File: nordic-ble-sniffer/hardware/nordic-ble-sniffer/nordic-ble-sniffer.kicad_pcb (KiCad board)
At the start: 2 copper layers, 8 parts, among them U1 NRF52840-QFAA-F-R7, U2 nRF52840, Y1 Crystal

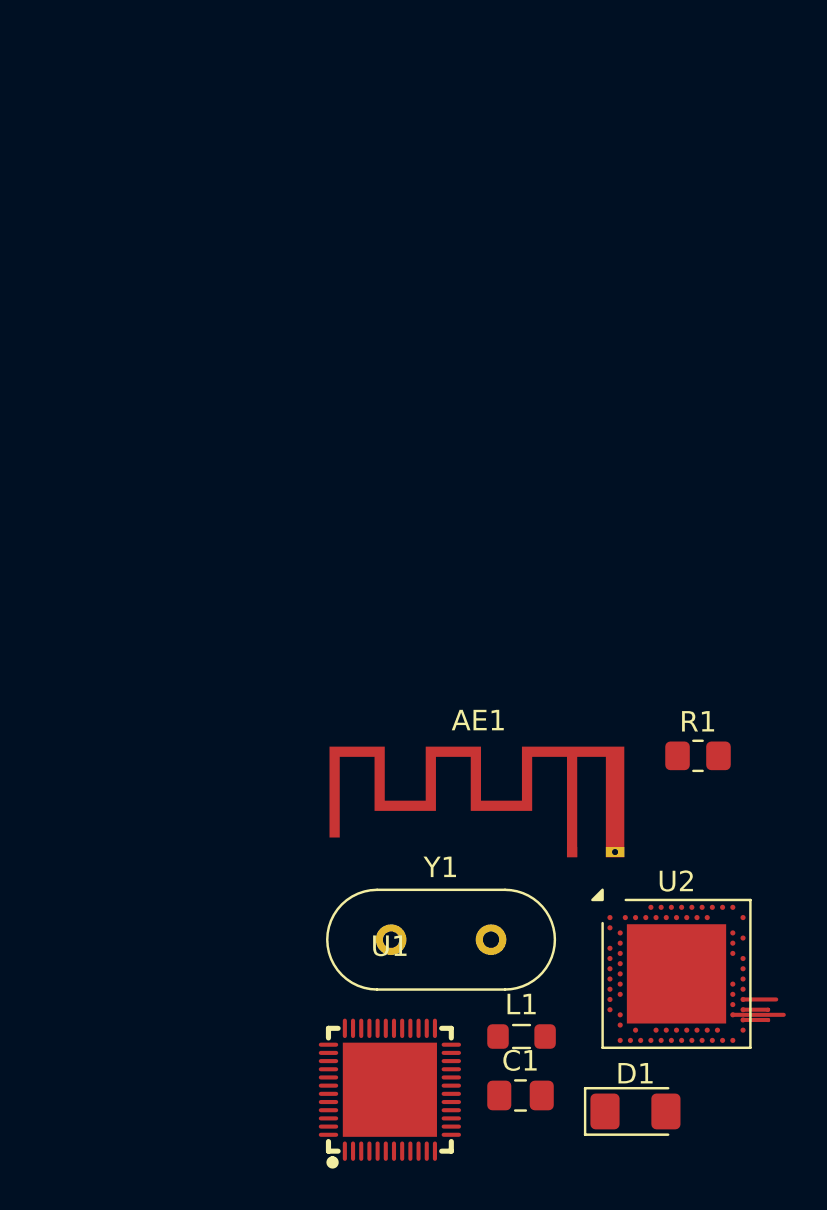
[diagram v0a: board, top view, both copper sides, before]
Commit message: finish schematic ble sniffer with nrf52833 qfn40
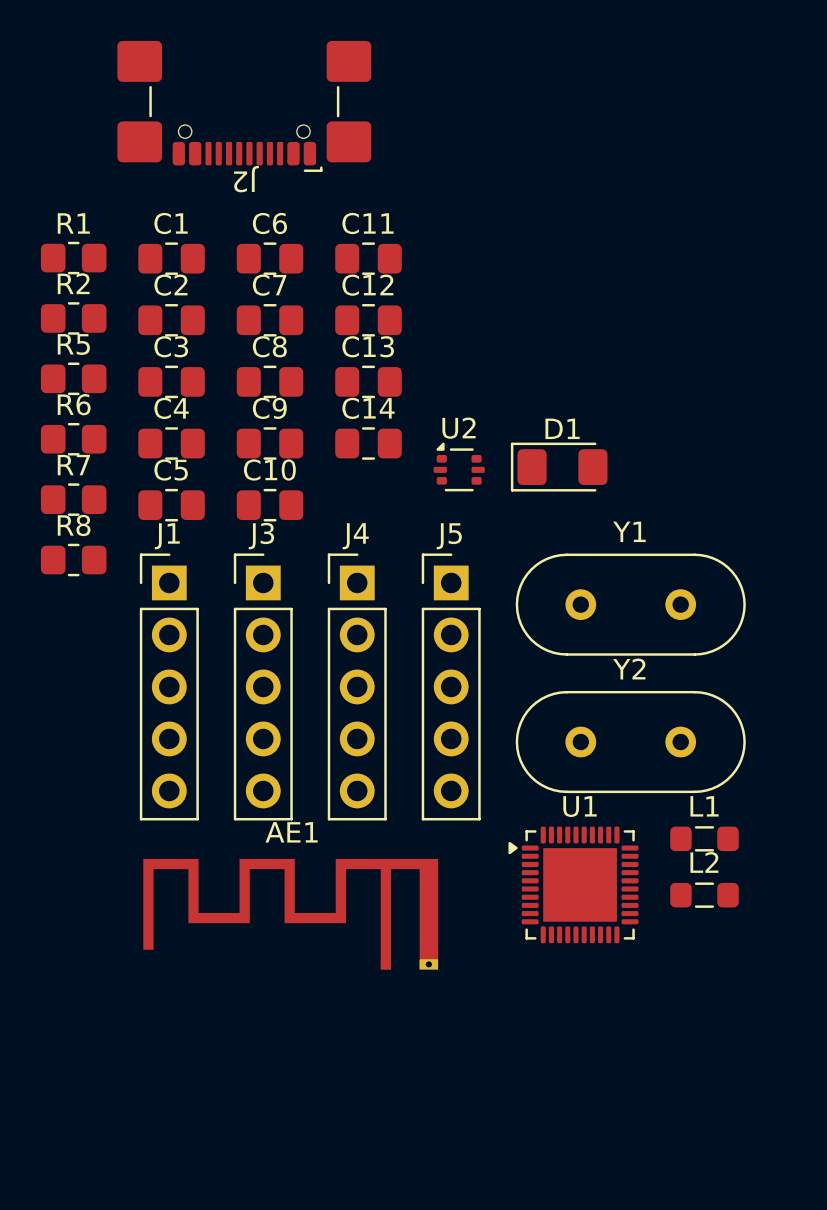
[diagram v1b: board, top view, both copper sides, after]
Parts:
- added C10: 4.7uF, Capacitor_SMD:C_0805_2012Metric_Pad1.18x1.45mm_HandSolder, F.Cu at (104.3, 63.7)
- added C11: 12pF, Capacitor_SMD:C_0805_2012Metric_Pad1.18x1.45mm_HandSolder, F.Cu at (109.1, 51.7)
- added C12: 12pF, Capacitor_SMD:C_0805_2012Metric_Pad1.18x1.45mm_HandSolder, F.Cu at (109.1, 54.7)
- added C13: 100nF, Capacitor_SMD:C_0805_2012Metric_Pad1.18x1.45mm_HandSolder, F.Cu at (109.1, 57.7)
- added C14: 100nF, Capacitor_SMD:C_0805_2012Metric_Pad1.18x1.45mm_HandSolder, F.Cu at (109.1, 60.7)
- added C2: 12pF, Capacitor_SMD:C_0805_2012Metric_Pad1.18x1.45mm_HandSolder, F.Cu at (99.5, 54.7)
- added C3: 12pF, Capacitor_SMD:C_0805_2012Metric_Pad1.18x1.45mm_HandSolder, F.Cu at (99.5, 57.7)
- added C4: 1pF, Capacitor_SMD:C_0805_2012Metric_Pad1.18x1.45mm_HandSolder, F.Cu at (99.5, 60.7)
- added C5: 1.2pF, Capacitor_SMD:C_0805_2012Metric_Pad1.18x1.45mm_HandSolder, F.Cu at (99.5, 63.7)
- added C6: 100nF, Capacitor_SMD:C_0805_2012Metric_Pad1.18x1.45mm_HandSolder, F.Cu at (104.3, 51.7)
- added C7: 820pF, Capacitor_SMD:C_0805_2012Metric_Pad1.18x1.45mm_HandSolder, F.Cu at (104.3, 54.7)
- added C8: 4.7uF, Capacitor_SMD:C_0805_2012Metric_Pad1.18x1.45mm_HandSolder, F.Cu at (104.3, 57.7)
- added C9: 4.7uF, Capacitor_SMD:C_0805_2012Metric_Pad1.18x1.45mm_HandSolder, F.Cu at (104.3, 60.7)
- added J1: gconn, Connector_PinHeader_2.54mm:PinHeader_1x05_P2.54mm_Vertical, F.Cu at (99.3, 67.5)
- added J2: USB2UART, Connector_USB:USB_C_Receptacle_GCT_USB4110, F.Cu at (103.0, 42.9)
- added J3: swd, Connector_PinHeader_2.54mm:PinHeader_1x05_P2.54mm_Vertical, F.Cu at (103.9, 67.5)
- added J4: gconn, Connector_PinHeader_2.54mm:PinHeader_1x05_P2.54mm_Vertical, F.Cu at (108.5, 67.5)
- added J5: gconn, Connector_PinHeader_2.54mm:PinHeader_1x05_P2.54mm_Vertical, F.Cu at (113.1, 67.5)
- added L2: 2.2nH, Inductor_SMD:L_0805_2012Metric_Pad1.05x1.20mm_HandSolder, F.Cu at (125.5, 82.8)
- added R2: 4K7, Resistor_SMD:R_0805_2012Metric_Pad1.20x1.40mm_HandSolder, F.Cu at (94.7, 54.6)
- added R5: 5K1, Resistor_SMD:R_0805_2012Metric_Pad1.20x1.40mm_HandSolder, F.Cu at (94.7, 57.6)
- added R6: 5K1, Resistor_SMD:R_0805_2012Metric_Pad1.20x1.40mm_HandSolder, F.Cu at (94.7, 60.5)
- added R7: 22 / 33, Resistor_SMD:R_0805_2012Metric_Pad1.20x1.40mm_HandSolder, F.Cu at (94.7, 63.5)
- added R8: 22 / 33, Resistor_SMD:R_0805_2012Metric_Pad1.20x1.40mm_HandSolder, F.Cu at (94.7, 66.4)
- added Y2: 32.768kHz, Crystal:Crystal_HC49-U_Vertical, F.Cu at (119.4, 75.3)
- C1: value C -> 100nF
- D1: value LED -> RED
- L1: value L -> 4.7nH
- R1: value R_US -> 10K
- U1: value NRF52840-QFAA-F-R7 -> nRF52833_QDxx; footprint easyeda2kicad:WQFN-48_L6.0-W6.0-P0.40-BL-EP4.6 -> Package_DFN_QFN:QFN-40-1EP_5x5mm_P0.4mm_EP3.6x3.6mm
- U2: value nRF52840 -> USBLC6-2P6; footprint Package_DFN_QFN:Nordic_AQFN-73-1EP_7x7mm_P0.5mm -> Package_TO_SOT_SMD:SOT-666
- Y1: value Crystal -> 32MHz
- moved C1 44.3 mm to (99.5, 51.7)
- moved R1 39.0 mm to (94.7, 51.7)
- moved D1 31.7 mm to (118.5, 61.9)
- moved U2 26.8 mm to (113.5, 62.0)
- moved Y1 18.8 mm to (119.4, 68.6)
- moved U1 13.7 mm to (119.4, 82.3)
- moved L1 13.2 mm to (125.5, 80.0)
- moved AE1 10.6 mm to (109.9, 86.2)
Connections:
- AE1 pad 1: unconnected-(AE1-A-Pad1) -> Net-(AE1-A)
- C1 pad 1: unconnected-(C1-Pad1) -> Net-(U1-DEC1)
- C1 pad 2: unconnected-(C1-Pad2) -> GND
- D1 pad 1: unconnected-(D1-K-Pad1) -> GND
- D1 pad 2: unconnected-(D1-A-Pad2) -> Net-(D1-A)
- L1 pad 1: unconnected-(L1-Pad1) -> Net-(C5-Pad1)
- L1 pad 2: unconnected-(L1-Pad2) -> Net-(U1-ANT)
- R1 pad 1: unconnected-(R1-Pad1) -> VBUS
- R1 pad 2: unconnected-(R1-Pad2) -> Net-(D1-A)
- U1 pad 1: unconnected-(U1-DEC1-Pad1) -> Net-(U1-DEC1)
- U1 pad 10: unconnected-(U1-P0.11/TRACEDATA2-Pad10) -> Net-(U1-VBUS)
- U1 pad 11: unconnected-(U1-P0.12/TRACEDATA1-Pad11) -> Net-(U1-DECUSB)
- U1 pad 12: unconnected-(U1-VDD-Pad12) -> /USB_DM
- U1 pad 13: unconnected-(U1-P0.13-Pad13) -> /USB_DP
- U1 pad 14: unconnected-(U1-P0.14-Pad14) -> /P0.15
- U1 pad 15: unconnected-(U1-P0.17-Pad15) -> /P0.17
- U1 pad 16: unconnected-(U1-P0.18/nRESET-Pad16) -> /RST
- U1 pad 17: unconnected-(U1-VDD-Pad17) -> /P0.20
- U1 pad 18: unconnected-(U1-P0.19-Pad18) -> VDD
- U1 pad 19: unconnected-(U1-P0.20-Pad19) -> /SWDIO
- U1 pad 2: unconnected-(U1-P0.00/XL1-Pad2) -> Net-(U1-XL1/P0.00)
- U1 pad 20: unconnected-(U1-P0.21-Pad20) -> /SWDCLK
- U1 pad 21: unconnected-(U1-P0.22-Pad21) -> Net-(U1-DEC5)
- U1 pad 22: unconnected-(U1-P0.23-Pad22) -> /NFC1/P0.09
- U1 pad 23: unconnected-(U1-P0.24-Pad23) -> /NFC2/P0.10
- U1 pad 24: unconnected-(U1-P1.00-Pad24) -> Net-(U1-ANT)
- U1 pad 25: unconnected-(U1-VDD-Pad25) -> GND
- U1 pad 26: unconnected-(U1-SWDIO-Pad26) -> Net-(U1-DEC4)
- U1 pad 27: unconnected-(U1-SWDCLK-Pad27) -> Net-(U1-DEC3)
- U1 pad 28: unconnected-(U1-NC-Pad28) -> Net-(U1-XC1)
- U1 pad 29: unconnected-(U1-P0.09/NFC1-Pad29) -> Net-(U1-XC2)
- U1 pad 3: unconnected-(U1-P0.01/XL2-Pad3) -> Net-(U1-XL2/P0.01)
- U1 pad 30: unconnected-(U1-P0.10/NFC2-Pad30) -> VDD
- U1 pad 31: unconnected-(U1-ANT-Pad31) -> /AIN1/P0.03
- U1 pad 32: unconnected-(U1-VSS_PA-Pad32) -> /AIN0/P0.02
- U1 pad 33: unconnected-(U1-DEC6-Pad33) -> /AIN4/P0.28
- U1 pad 34: unconnected-(U1-DEC3-Pad34) -> /AIN5/P0.29
- U1 pad 35: unconnected-(U1-XC1-Pad35) -> /AIN6/P0.30
- U1 pad 36: unconnected-(U1-XC2-Pad36) -> /AIN7/P0.31
- U1 pad 37: unconnected-(U1-VDD-Pad37) -> GND
- U1 pad 38: unconnected-(U1-P1.15-Pad38) -> Net-(U1-DEC4)
- U1 pad 4: unconnected-(U1-P0.04/AIN2-Pad4) -> /AIN2/P0.04
- U1 pad 40: unconnected-(U1-P0.02/AIN0-Pad40) -> VDD
- U1 pad 41: unconnected-(U1-P0.28/AIN4-Pad41) -> GND
- U1 pad 5: unconnected-(U1-P0.05/AIN3-Pad5) -> /AIN3/P0.05
- U1 pad 6: unconnected-(U1-P0.07/TRACECLK-Pad6) -> /P1.09
- U1 pad 7: unconnected-(U1-P0.08-Pad7) -> /P0.11
- U1 pad 8: unconnected-(U1-P1.08-Pad8) -> VDD
- U1 pad 9: unconnected-(U1-P1.09/TRACEDATA3-Pad9) -> Net-(U1-VBUS)
- Y1 pad 1: unconnected-(Y1-Pad1) -> Net-(U1-XC1)
- Y1 pad 2: unconnected-(Y1-Pad2) -> Net-(U1-XC2)
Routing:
- net unconnected-(U2-P1.01-PadY23): track 2.49 -> 0.00 mm
- net unconnected-(U2-P1.04-PadU24): track 1.62 -> 0.00 mm
- net unconnected-(U2-SWDCLK-PadAA24): track 1.23 -> 0.00 mm
- net unconnected-(U2-P1.02-PadW24): track 1.23 -> 0.00 mm

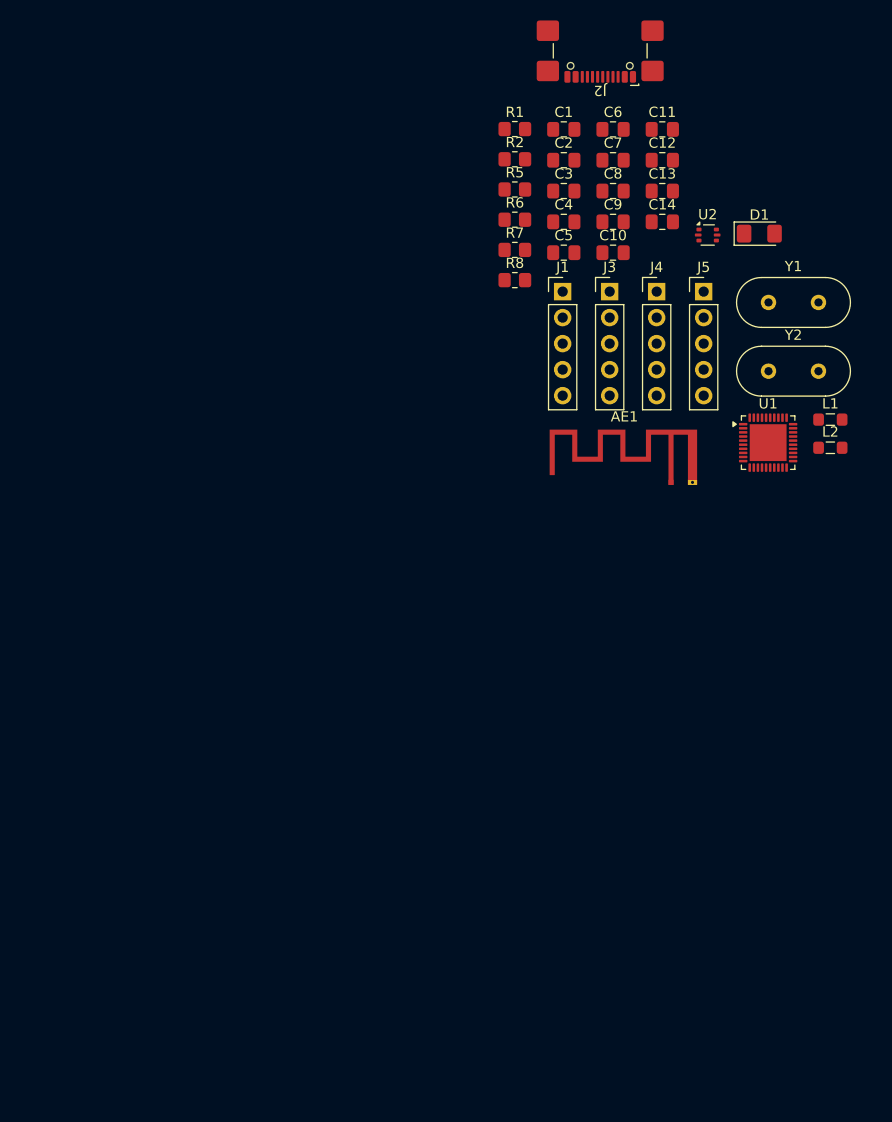
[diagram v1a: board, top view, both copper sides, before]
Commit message: finish ble-sniffer routing but excluding dummy pin header
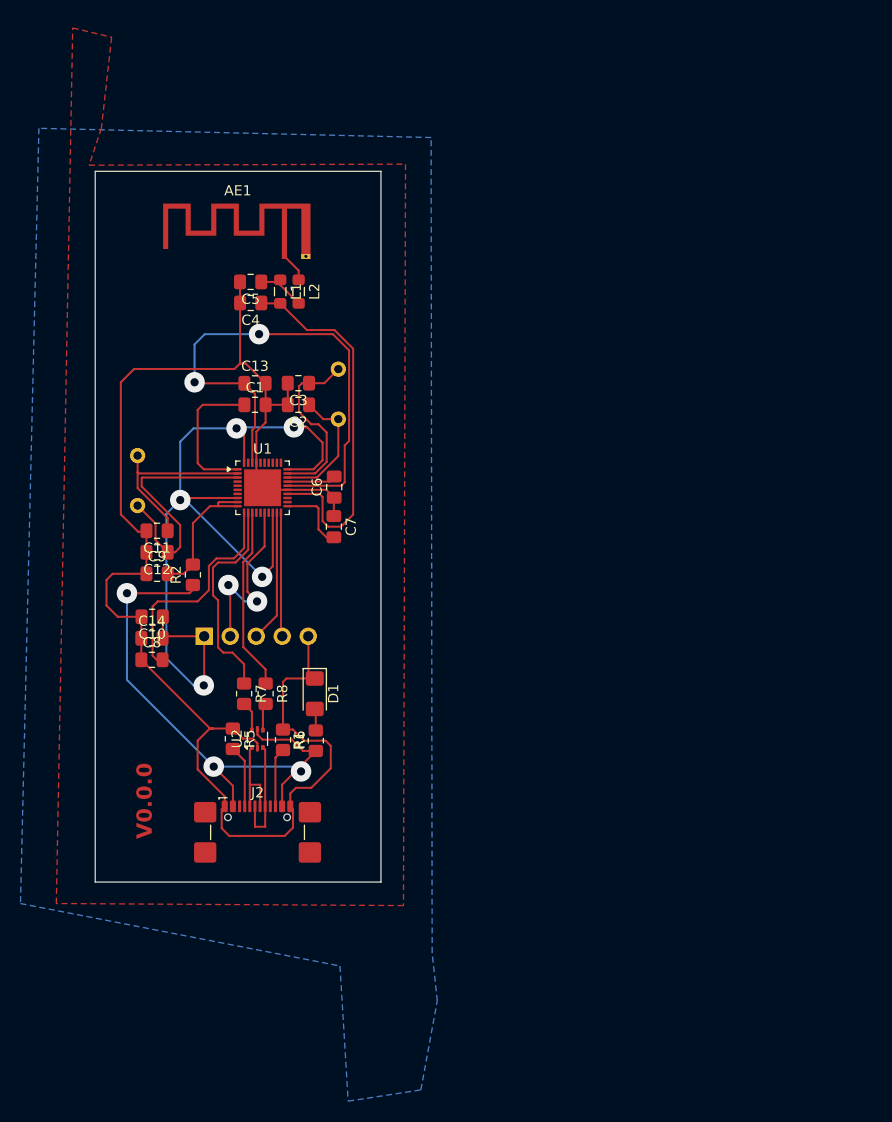
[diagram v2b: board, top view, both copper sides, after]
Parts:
- removed J1, J4, J5: gconn, Connector_PinHeader_2.54mm:PinHeader_1x05_P2.54mm_Vertical
- J3, Y1, Y2: moved to B.Cu
- moved J2 85.4 mm to (69.5, 121.5), turned to 0 degrees
- moved U2 66.0 mm to (69.5, 111.2), turned to 90 degrees
- moved C14 64.3 mm to (59.2, 101.4)
- moved C8 64.2 mm to (59.2, 103.5)
- moved C11 63.0 mm to (59.7, 90.9), turned to 180 degrees
- moved R1 62.8 mm to (75.2, 111.4), turned to 90 degrees
- moved D1 62.5 mm to (75.1, 106.8), turned to -90 degrees
- moved C12 62.4 mm to (59.7, 93.0), turned to 180 degrees
- moved Y2 62.2 mm to (57.8, 83.6), turned to -90 degrees
- moved R5 60.3 mm to (67.1, 111.2), turned to -90 degrees
- moved C10 57.4 mm to (59.3, 99.3), turned to 180 degrees
- moved C9 56.2 mm to (59.7, 95.1)
- moved R6 55.6 mm to (72.0, 111.3), turned to -90 degrees
- moved L1 55.2 mm to (71.8, 67.5), turned to -90 degrees
- moved L2 54.1 mm to (73.6, 67.5), turned to -90 degrees
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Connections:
- J3 pad 3: /SWDCLK -> /SWDIO
- J3 pad 4: /SWDIO -> /SWDCLK
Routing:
- net GND: track 0.00 -> 146.9 mm
- net VDD: track 0.00 -> 85.3 mm, vias 0 -> 5
- net VBUS: track 0.00 -> 54.5 mm, vias 0 -> 3
- net Net-(U1-DEC4): track 0.00 -> 51.8 mm, vias 0 -> 2
- net Net-(U1-ANT): track 0.00 -> 36.6 mm
- net Net-(U1-XL2/P0.01): track 0.00 -> 24.9 mm
- net Net-(U1-DECUSB): track 0.00 -> 22.1 mm
- net /USB_DM: track 0.00 -> 21.1 mm
- net /RST: track 0.00 -> 18.4 mm, vias 0 -> 2
- net Net-(U1-XL1/P0.00): track 0.00 -> 18.4 mm
- net /USB_DP: track 0.00 -> 17.9 mm
- net Net-(U1-XC2): track 0.00 -> 17.7 mm
- net Net-(U1-VBUS): track 0.00 -> 14.2 mm
- net Net-(U1-DEC1): track 0.00 -> 14.1 mm
- net /SWDIO: track 0.00 -> 12.9 mm
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- added copper zone on B.Cu, net (none)
- added copper zone on F.Cu, net (none)
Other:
- board outline added: 27.9 x 69.4 mm
- board text added: "V0.0.0"
